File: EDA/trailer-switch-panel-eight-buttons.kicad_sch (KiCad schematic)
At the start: 41 parts, among them IC1 AP63203WU-7, J1 Conn_01x06, J2 Conn_01x04, SW1 SW_Push, SW2 SW_Push, SW3 SW_Push, SW4 SW_Push, SW5 SW_Push, SW6 SW_Push, SW7 SW_Push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

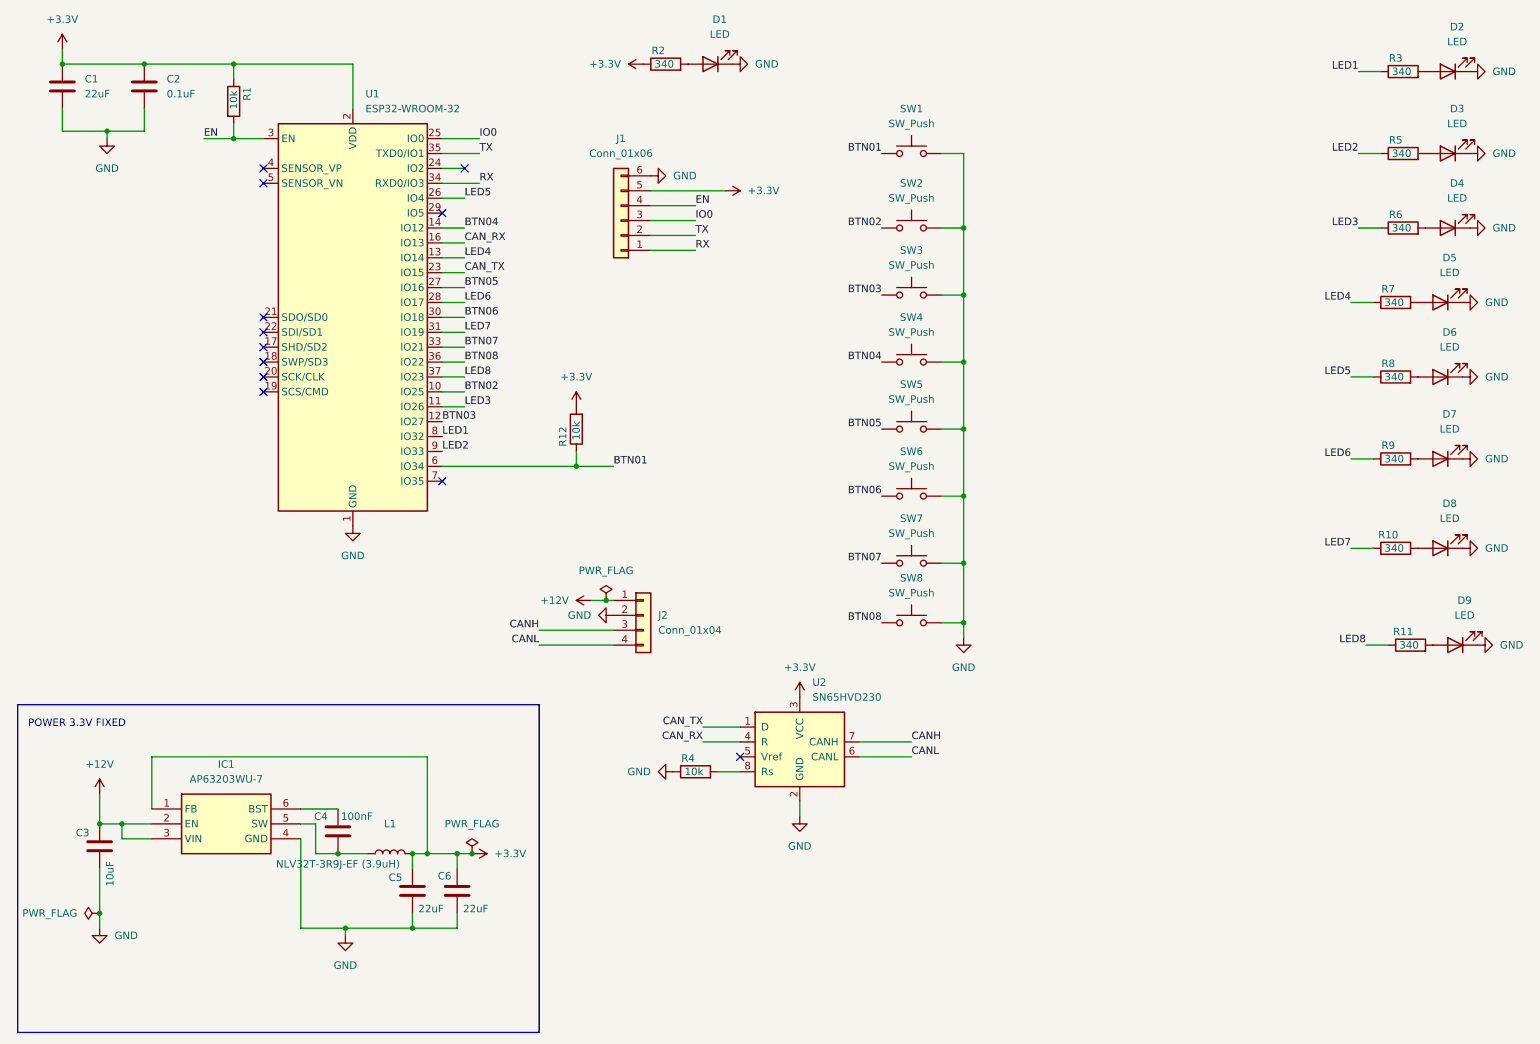
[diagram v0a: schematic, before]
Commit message: Updated PCB to use JST XH connectors
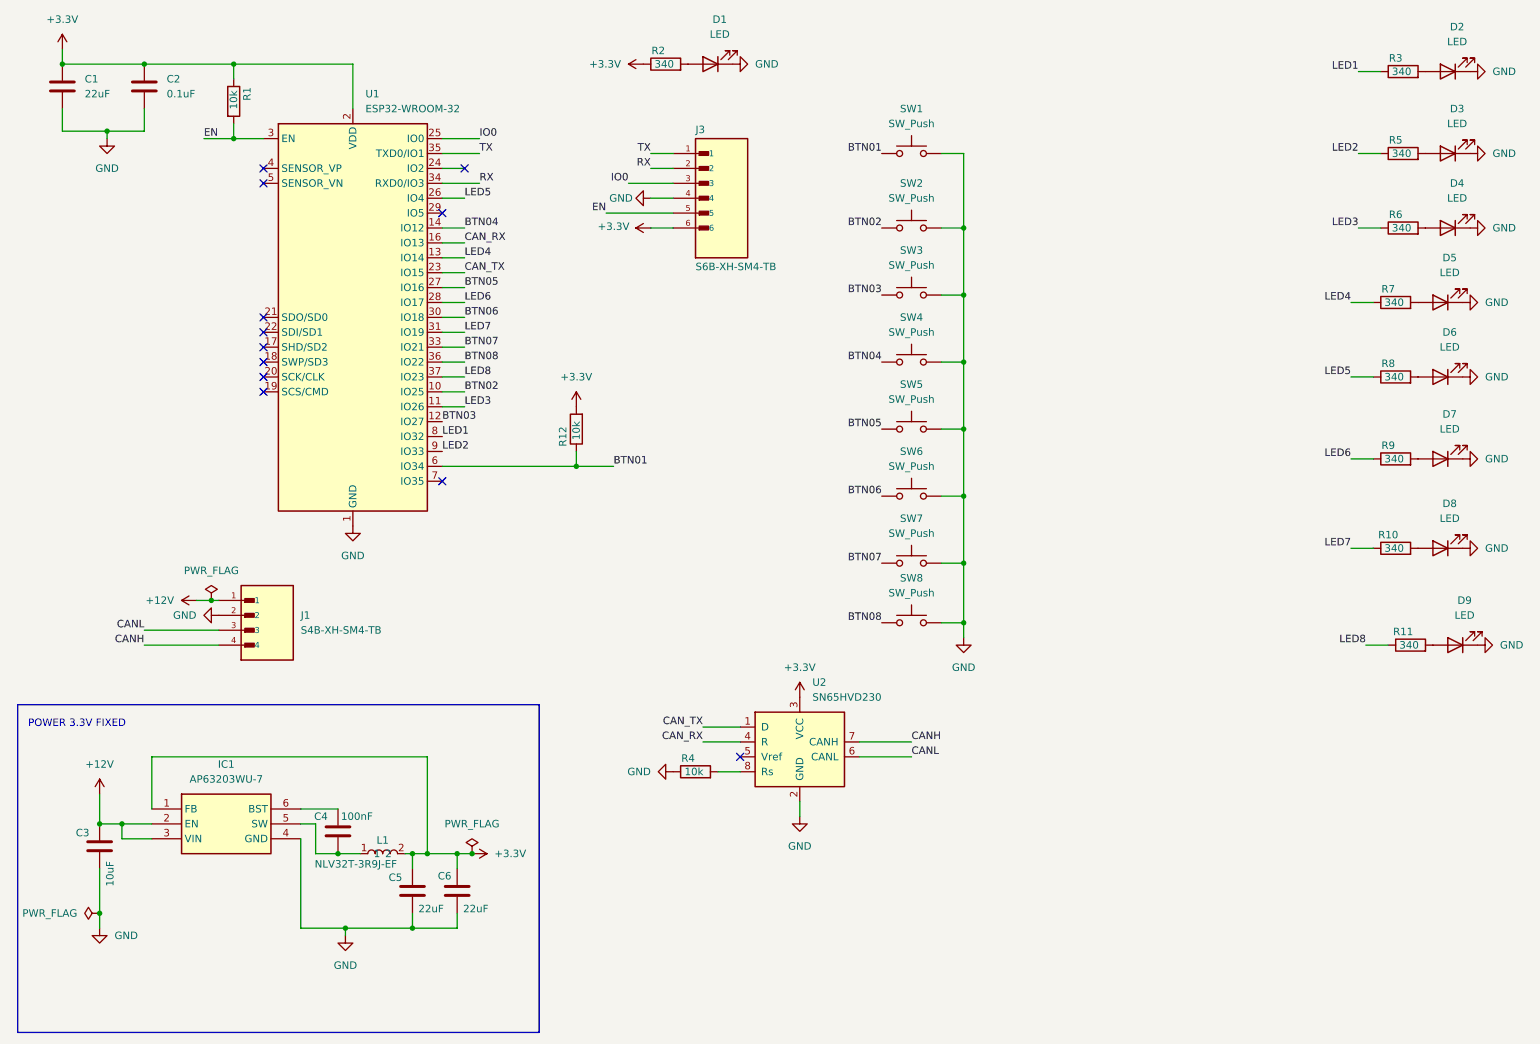
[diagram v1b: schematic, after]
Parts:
- removed IC1: AP63203WU-7, CustomLibraries:AP63203WU7, symbol Converter_DCDC:AP63203WU-7
- removed J1: Conn_01x06, Connector_PinHeader_2.54mm:PinHeader_1x06_P2.54mm_Horizontal, symbol Connector_Generic:Conn_01x06
- removed J2: Conn_01x04, CustomLibraries:CAN_PLUS_POWER, symbol Connector_Generic:Conn_01x04
- removed L1: NLV32T-3R9J-EF (3.9uH), CustomLibraries:INDM3225X240N, symbol Device:L
- added IC1: AP63203WU-7, TrailCurrentFootprints:AP63203WU7, symbol TrailCurrentSymbolLibrary:AP63203WU-7
- added J1: S4B-XH-SM4-TB, TrailCurrentFootprints:JST_S4B-XH-SM4-TB, symbol TrailCurrentSymbolLibrary:S4B-XH-SM4-TB
- added J3: S6B-XH-SM4-TB, TrailCurrentFootprints:JST_S6B-XH-SM4-TB, symbol TrailCurrentSymbolLibrary:S6B-XH-SM4-TB
- added L1: NLV32T-3R9J-EF, TrailCurrentFootprints:NLV32T-3R9J-EF, symbol TrailCurrentSymbolLibrary:NLV32T-3R9J-EF
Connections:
- net +12V: now also IC1.2 (EN), IC1.3 (VIN), J1.1
- net +3.3V: now also IC1.1 (FB), J3.6, L1.2
- net CANH: now also J1.4
- net CANL: now also J1.3
- net EN: now also J3.5
- net GND: now also IC1.4 (GND), J1.2, J3.4
- net IO0: now also J3.3
- net RX: now also J3.2
- net TX: now also J3.1
- net at C4.2: now also IC1.5 (SW), L1.1
- net at C4.1: now also IC1.6 (BST)

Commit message: Added DIP switch for CAN Termination and device ID settings
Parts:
- added R13: 120, Resistor_SMD:R_1206_3216Metric_Pad1.30x1.75mm_HandSolder, symbol Device:R
- added R14, R15, R16: 10k, Resistor_SMD:R_1206_3216Metric_Pad1.30x1.75mm_HandSolder, symbol Device:R
- added SW9: DS-04, TrailCurrentFootprints:DS-04, symbol TrailCurrentSymbolLibrary:DS-04
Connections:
- net +3.3V: now also R14.2, R15.2, R16.2
- net CANH: now also R13.1
- net CANL: now also SW9.4
- net GND: now also SW9.5, SW9.6, SW9.7
- net ADDR02: now reaches U1.4 (SENSOR_VP)
- net ADDR02: now also R15.1, SW9.2
- net ADDR01: now reaches U1.5 (SENSOR_VN)
- net ADDR01: now also R16.1, SW9.3
- net ADDR03: now reaches U1.7 (IO35)
- net ADDR03: now also R14.1, SW9.1
- new net: R13.2, SW9.8
- no-connect marks 12 -> 9
